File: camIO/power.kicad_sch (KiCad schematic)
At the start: 5 parts, among them IC3 TLV61225DC

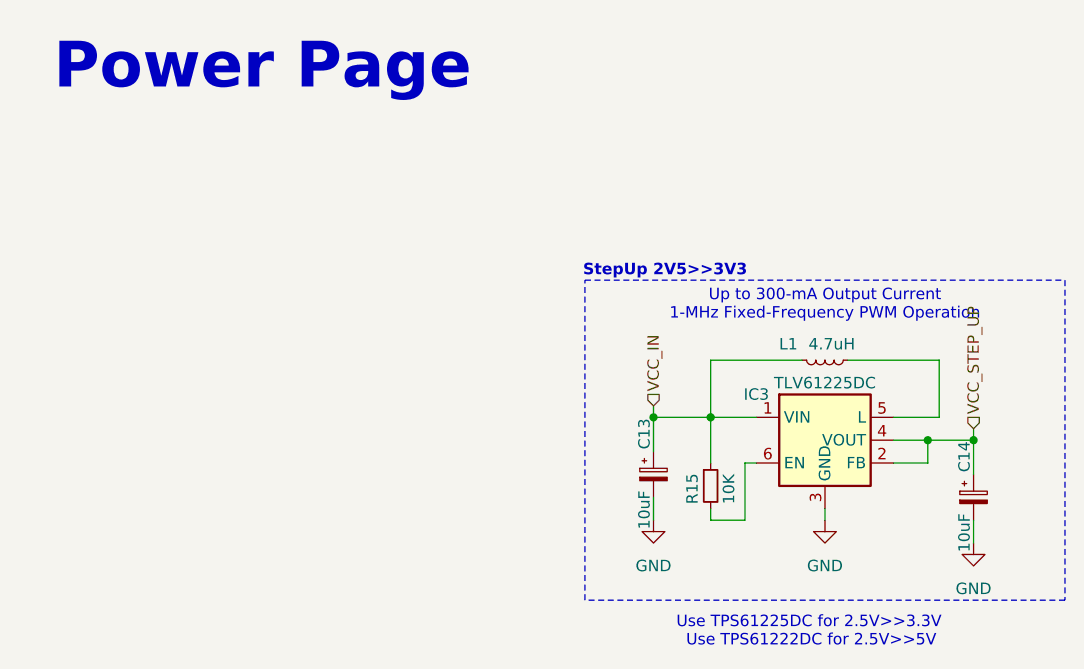
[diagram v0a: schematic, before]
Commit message: sch cleanup - reference cleanup
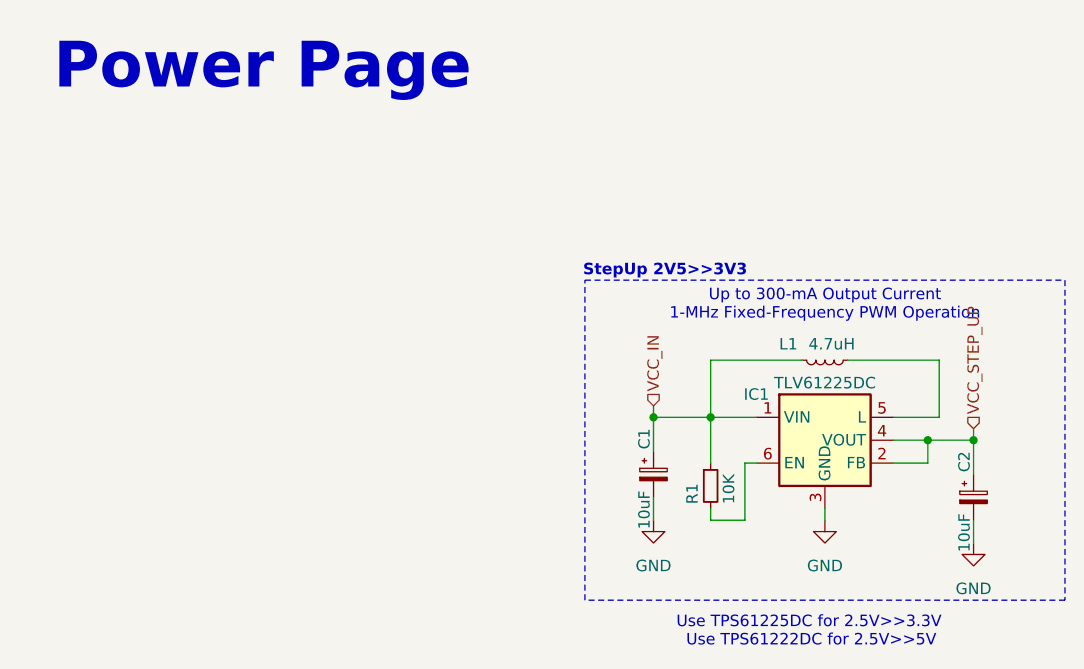
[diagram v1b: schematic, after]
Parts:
- renumbered C13 to C1, C14 to C2, IC3 to IC1, R15 to R1
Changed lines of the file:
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@@
 		(on_board yes)
 		(dnp no)
-		(property "Reference" "R15"
+		(property "Reference" "R1"
 			(at 83.058 65.532 90)
 			(effects
@@
 			(project "extension_template"
 				(path "/771d591f-f69b-4219-83f3-922c3a7e343e/f0eb6774-d49a-4b74-88fc-55da30cd877c/cc4b169f-4dc5-49c3-9327-bc1152f2123a"
-					(reference "R15")
+					(reference "R1")
 					(unit 1)
 				)
@@
 		(on_board yes)
 		(dnp no)
-		(property "Reference" "IC3"
+		(property "Reference" "IC1"
 			(at 90.17 53.34 0)
 			(effects
@@
 			(project "extension_template"
 				(path "/771d591f-f69b-4219-83f3-922c3a7e343e/f0eb6774-d49a-4b74-88fc-55da30cd877c/cc4b169f-4dc5-49c3-9327-bc1152f2123a"
-					(reference "IC3")
+					(reference "IC1")
 					(unit 1)
 				)
@@
 		(on_board yes)
 		(dnp no)
-		(property "Reference" "C13"
+		(property "Reference" "C1"
 			(at 77.724 59.436 90)
 			(effects
@@
 			(project "extension_template"
 				(path "/771d591f-f69b-4219-83f3-922c3a7e343e/f0eb6774-d49a-4b74-88fc-55da30cd877c/cc4b169f-4dc5-49c3-9327-bc1152f2123a"
-					(reference "C13")
+					(reference "C1")
 					(unit 1)
 				)
@@
 		(on_board yes)
 		(dnp no)
-		(property "Reference" "C14"
+		(property "Reference" "C2"
 			(at 113.284 61.976 90)
 			(effects
@@
 			(project "extension_template"
 				(path "/771d591f-f69b-4219-83f3-922c3a7e343e/f0eb6774-d49a-4b74-88fc-55da30cd877c/cc4b169f-4dc5-49c3-9327-bc1152f2123a"
-					(reference "C14")
-					(unit 1)
-				)
+					(reference "C2")
+					(unit 1)
+				)
